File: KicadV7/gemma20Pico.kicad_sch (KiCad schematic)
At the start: 14 parts, among them J1-Prox1 I2C_CH0, J2-Prox0 I2C_CH1, J3-Motor1 DC-Motor, J4-BAT1 3.7V Battery, J5-Servo1 Servo, J6-Pot1 Pot, J7-Pot2 Pot, M1 Motor_DC, M2 Motor_Servo, U1-RPI-Pico1 Pico

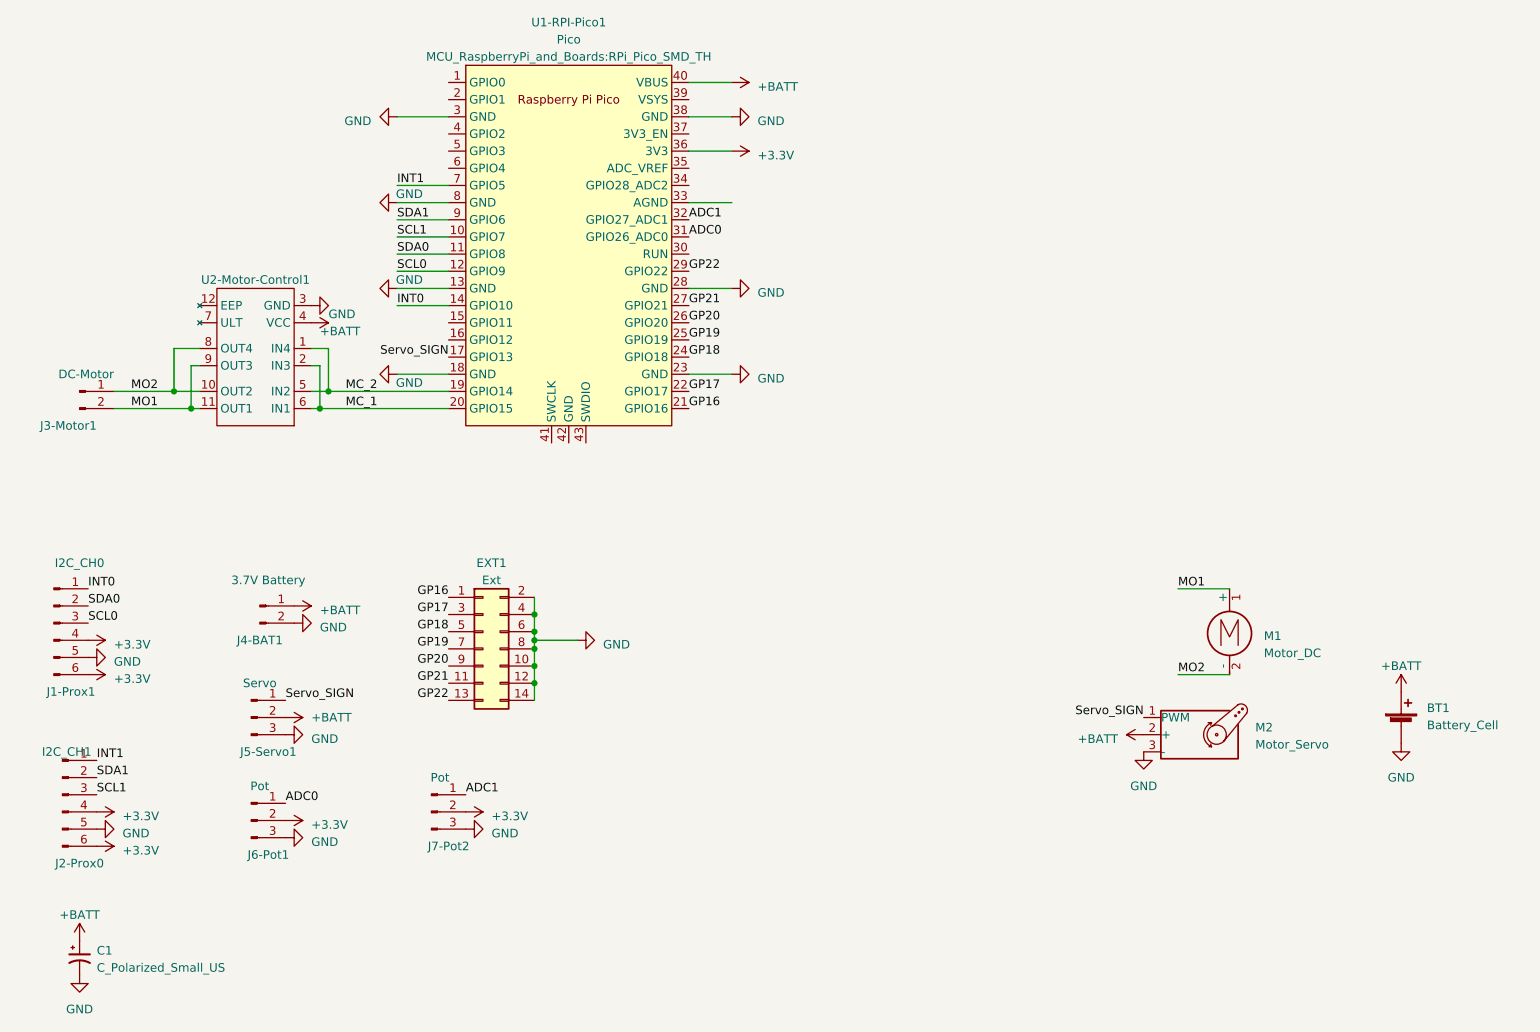
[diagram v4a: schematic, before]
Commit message: Added ECS Pins & cleanup
Added ECS connector allows the DRV8833 to be replaced  with brushless motor controller for RC (also provides +5v)
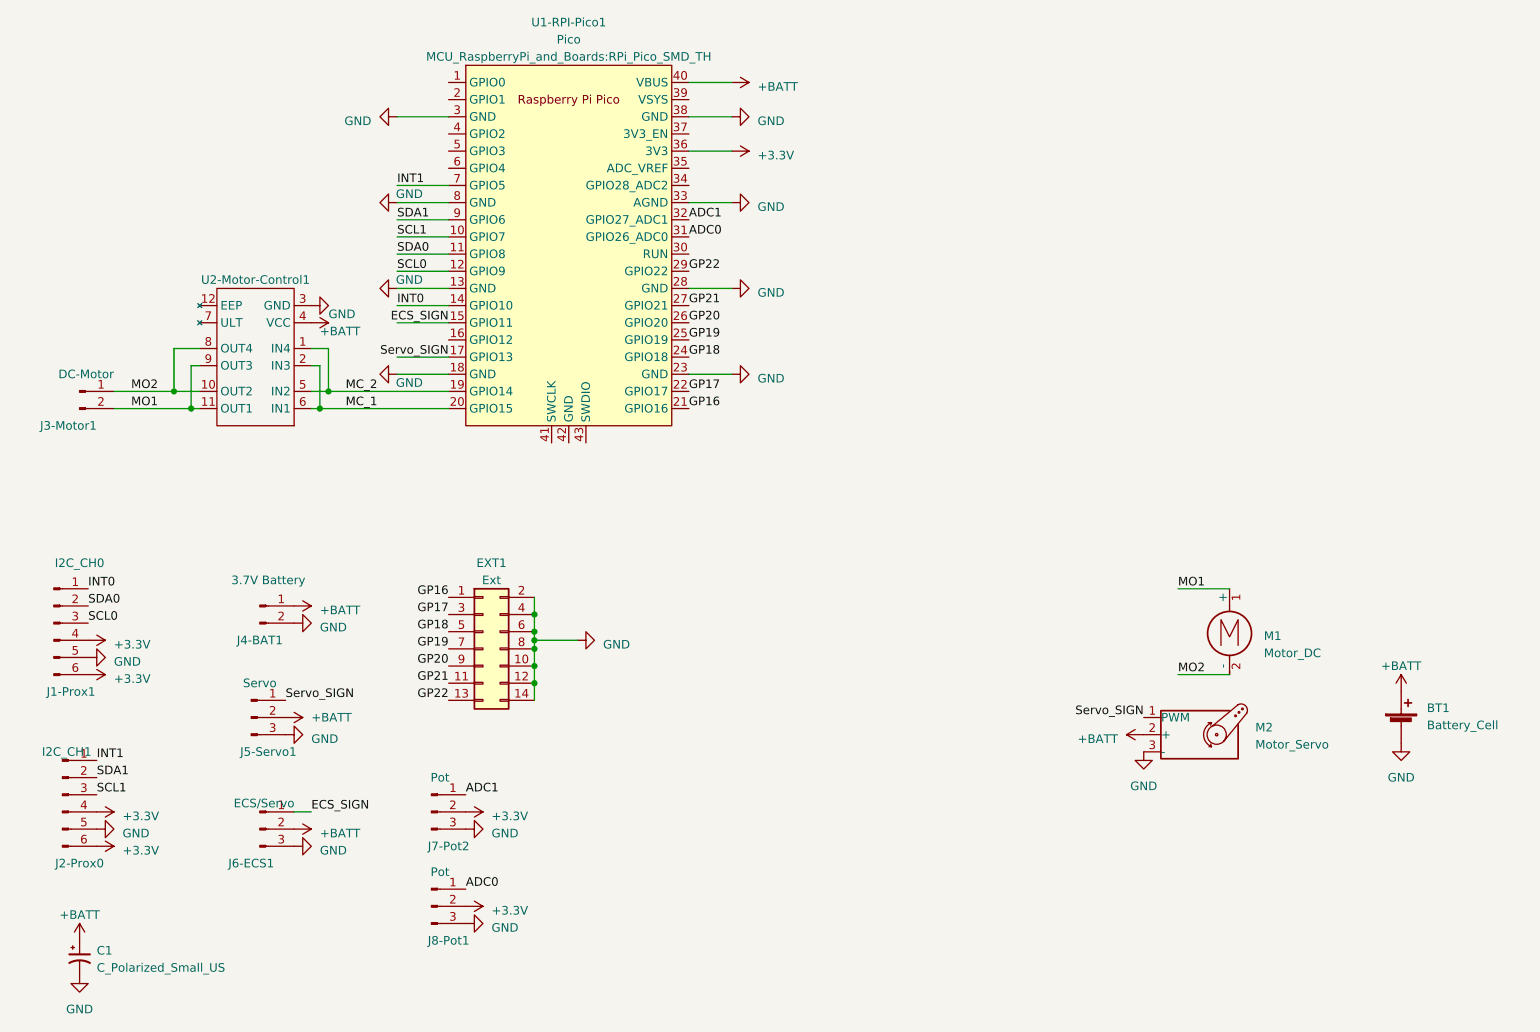
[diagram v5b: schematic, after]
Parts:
- added J6-ECS1: ECS/Servo, Connector_PinHeader_2.54mm:PinHeader_1x03_P2.54mm_Vertical, symbol Connector:Conn_01x03_Pin
- renumbered J6-Pot1 to J8-Pot1
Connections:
- net +BATT: now also J6-ECS1.2 (Pin_2)
- net GND: now also U1-RPI-Pico1.33 (AGND), J6-ECS1.3 (Pin_3)
- net ECS_SIGN: now reaches U1-RPI-Pico1.15 (GPIO11)
- net ECS_SIGN: now also J6-ECS1.1 (Pin_1)
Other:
- moved on the sheet: J8-Pot1
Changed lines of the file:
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@@
+    (stroke (width 0) (type default))
+  )
+  (wire (pts (xy 86.36 83.82) (xy 93.98 83.82))
     (stroke (width 0) (type default))
   )
@@
     (stroke (width 0) (type default))
   )
+  (wire (pts (xy 71.12 151.13) (xy 73.66 151.13))
+    (stroke (width 0) (type default))
+  )
   (wire (pts (xy 76.2 88.9) (xy 93.98 88.9))
     (stroke (width 0) (type default))
@@
   )
   (wire (pts (xy 86.36 71.12) (xy 93.98 71.12))
+    (stroke (width 0) (type default))
+  )
+  (wire (pts (xy 86.36 78.74) (xy 93.98 78.74))
     (stroke (width 0) (type default))
   )
@@
     (effects (font (size 1.27 1.27)) (justify left bottom))
   )
+  (label "ECS_SIGN" (at 93.98 78.74 180) (fields_autoplaced)
+    (effects (font (size 1.27 1.27)) (justify right bottom))
+  )
   (label "GP20" (at 129.54 78.74 0) (fields_autoplaced)
     (effects (font (size 1.27 1.27)) (justify left bottom))
@@
     (effects (font (size 1.27 1.27)) (justify left bottom))
   )
+  (label "ECS_SIGN" (at 73.66 151.13 0) (fields_autoplaced)
+    (effects (font (size 1.27 1.27)) (justify left bottom))
+  )
   (label "INT1" (at 86.36 58.42 0) (fields_autoplaced)
     (effects (font (size 1.27 1.27)) (justify left bottom))
@@
     (effects (font (size 1.27 1.27)) (justify left bottom))
   )
-  (label "ADC0" (at 69.85 149.86 0) (fields_autoplaced)
+  (label "ADC0" (at 96.52 162.56 0) (fields_autoplaced)
     (effects (font (size 1.27 1.27)) (justify left bottom))
   )
@@
     )
   )
-  (symbol (lib_id "power:+3.3V") (at 69.85 152.4 270) (unit 1)
-    (in_bom yes) (on_board yes) (dnp no) (fields_autoplaced)
-    (property "Reference" "#PWR020" (at 66.04 152.4 0)
-      (effects (font (size 1.27 1.27)) hide)
-    )
-    (property "Value" "+3.3V" (at 73.66 153.035 90)
-      (effects (font (size 1.27 1.27)) (justify left))
-    )
-    (property "Footprint" "" (at 69.85 152.4 0)
-      (effects (font (size 1.27 1.27)) hide)
-    )
-    (property "Datasheet" "" (at 69.85 152.4 0)
+  (symbol (lib_id "power:+3.3V") (at 96.52 165.1 270) (unit 1)
+    (in_bom yes) (on_board yes) (dnp no) (fields_autoplaced)
+    (property "Reference" "#PWR020" (at 92.71 165.1 0)
+      (effects (font (size 1.27 1.27)) hide)
+    )
+    (property "Value" "+3.3V" (at 100.33 165.735 90)
+      (effects (font (size 1.27 1.27)) (justify left))
+    )
+    (property "Footprint" "" (at 96.52 165.1 0)
+      (effects (font (size 1.27 1.27)) hide)
+    )
+    (property "Datasheet" "" (at 96.52 165.1 0)
       (effects (font (size 1.27 1.27)) hide)
     )
@@
     )
   )
+  (symbol (lib_id "power:+BATT") (at 71.12 153.67 270) (unit 1)
+    (in_bom yes) (on_board yes) (dnp no) (fields_autoplaced)
+    (property "Reference" "#PWR033" (at 67.31 153.67 0)
+      (effects (font (size 1.27 1.27)) hide)
+    )
+    (property "Value" "+BATT" (at 74.93 154.305 90)
+      (effects (font (size 1.27 1.27)) (justify left))
+    )
+    (property "Footprint" "" (at 71.12 153.67 0)
+      (effects (font (size 1.27 1.27)) hide)
+    )
+    (property "Datasheet" "" (at 71.12 153.67 0)
+      (effects (font (size 1.27 1.27)) hide)
+    )
+    (pin "1")
+    (instances
+      (project "gemma20Pico"
+        (path "/b10b7441-68fa-49c0-9dad-fceb534010fc"
+          (reference "#PWR033") (unit 1)
+        )
+      )
+    )
+  )
   (symbol (lib_id "power:GND") (at 86.36 86.36 270) (unit 1)
     (in_bom yes) (on_board yes) (dnp no)
@@
     )
   )
+  (symbol (lib_id "power:GND") (at 135.89 60.96 90) (unit 1)
+    (in_bom yes) (on_board yes) (dnp no) (fields_autoplaced)
+    (property "Reference" "#PWR035" (at 142.24 60.96 0)
+      (effects (font (size 1.27 1.27)) hide)
+    )
+    (property "Value" "GND" (at 139.7 61.595 90)
+      (effects (font (size 1.27 1.27)) (justify right))
+    )
+    (property "Footprint" "" (at 135.89 60.96 0)
+      (effects (font (size 1.27 1.27)) hide)
+    )
+    (property "Datasheet" "" (at 135.89 60.96 0)
+      (effects (font (size 1.27 1.27)) hide)
+    )
+    (pin "1")
+    (instances
+      (project "gemma20Pico"
+        (path "/b10b7441-68fa-49c0-9dad-fceb534010fc"
+          (reference "#PWR035") (unit 1)
+        )
+      )
+    )
+  )
   (symbol (lib_id "power:GND") (at 86.36 60.96 270) (unit 1)
     (in_bom yes) (on_board yes) (dnp no)
@@
     )
   )
-  (symbol (lib_id "Connector:Conn_01x03_Pin") (at 64.77 152.4 0) (unit 1)
-    (in_bom yes) (on_board yes) (dnp no)
-    (property "Reference" "J6-Pot1" (at 67.31 157.48 0)
-      (effects (font (size 1.27 1.27)))
-    )
-    (property "Value" "Pot" (at 66.04 147.32 0)
-      (effects (font (size 1.27 1.27)))
-    )
-    (property "Footprint" "Connector_PinSocket_2.54mm:PinSocket_1x03_P2.54mm_Vertical" (at 64.77 152.4 0)
-      (effects (font (size 1.27 1.27)) hide)
-    )
-    (property "Datasheet" "~" (at 64.77 152.4 0)
+  (symbol (lib_id "Connector:Conn_01x03_Pin") (at 91.44 165.1 0) (unit 1)
+    (in_bom yes) (on_board yes) (dnp no)
+    (property "Reference" "J8-Pot1" (at 93.98 170.18 0)
+      (effects (font (size 1.27 1.27)))
+    )
+    (property "Value" "Pot" (at 92.71 160.02 0)
+      (effects (font (size 1.27 1.27)))
+    )
+    (property "Footprint" "Connector_PinSocket_2.54mm:PinSocket_1x03_P2.54mm_Vertical" (at 91.44 165.1 0)
+      (effects (font (size 1.27 1.27)) hide)
+    )
+    (property "Datasheet" "~" (at 91.44 165.1 0)
       (effects (font (size 1.27 1.27)) hide)
     )
@@
       (project "gemma20Pico"
         (path "/b10b7441-68fa-49c0-9dad-fceb534010fc"
-          (reference "J6-Pot1") (unit 1)
+          (reference "J8-Pot1") (unit 1)
         )
       )
@@
     )
   )
+  (symbol (lib_id "power:GND") (at 71.12 156.21 90) (unit 1)
+    (in_bom yes) (on_board yes) (dnp no) (fields_autoplaced)
+    (property "Reference" "#PWR034" (at 77.47 156.21 0)
+      (effects (font (size 1.27 1.27)) hide)
+    )
+    (property "Value" "GND" (at 74.93 156.845 90)
+      (effects (font (size 1.27 1.27)) (justify right))
+    )
+    (property "Footprint" "" (at 71.12 156.21 0)
+      (effects (font (size 1.27 1.27)) hide)
+    )
+    (property "Datasheet" "" (at 71.12 156.21 0)
+      (effects (font (size 1.27 1.27)) hide)
+    )
+    (pin "1")
+    (instances
+      (project "gemma20Pico"
+        (path "/b10b7441-68fa-49c0-9dad-fceb534010fc"
+          (reference "#PWR034") (unit 1)
+        )
+      )
+    )
+  )
   (symbol (lib_id "Connector:Conn_01x02_Pin") (at 66.04 120.65 0) (unit 1)
     (in_bom yes) (on_board yes) (dnp no)
@@
     )
   )
-  (symbol (lib_id "power:GND") (at 69.85 154.94 90) (unit 1)
-    (in_bom yes) (on_board yes) (dnp no) (fields_autoplaced)
-    (property "Reference" "#PWR021" (at 76.2 154.94 0)
-      (effects (font (size 1.27 1.27)) hide)
-    )
-    (property "Value" "GND" (at 73.66 155.575 90)
-      (effects (font (size 1.27 1.27)) (justify right))
-    )
-    (property "Footprint" "" (at 69.85 154.94 0)
-      (effects (font (size 1.27 1.27)) hide)
-    )
-    (property "Datasheet" "" (at 69.85 154.94 0)
+  (symbol (lib_id "power:GND") (at 96.52 167.64 90) (unit 1)
+    (in_bom yes) (on_board yes) (dnp no) (fields_autoplaced)
+    (property "Reference" "#PWR021" (at 102.87 167.64 0)
+      (effects (font (size 1.27 1.27)) hide)
+    )
+    (property "Value" "GND" (at 100.33 168.275 90)
+      (effects (font (size 1.27 1.27)) (justify right))
+    )
+    (property "Footprint" "" (at 96.52 167.64 0)
+      (effects (font (size 1.27 1.27)) hide)
+    )
+    (property "Datasheet" "" (at 96.52 167.64 0)
       (effects (font (size 1.27 1.27)) hide)
     )
@@
         )
       )
+    )
+  )
+  (symbol (lib_id "Connector:Conn_01x03_Pin") (at 66.04 153.67 0) (unit 1)
+    (in_bom yes) (on_board yes) (dnp no)
+    (property "Reference" "J6-ECS1" (at 64.77 158.75 0)
+      (effects (font (size 1.27 1.27)))
+    )
+    (property "Value" "ECS/Servo" (at 66.675 149.86 0)
+      (effects (font (size 1.27 1.27)))
+    )
+    (property "Footprint" "Connector_PinHeader_2.54mm:PinHeader_1x03_P2.54mm_Vertical" (at 66.04 153.67 0)
+      (effects (font (size 1.27 1.27)) hide)
+    )
+    (property "Datasheet" "~" (at 66.04 153.67 0)
+      (effects (font (size 1.27 1.27)) hide)
+    )
+    (pin "1")
+    (pin "2")
+    (pin "3")
+    (instances
+      (project "gemma20Pico"
+        (path "/b10b7441-68fa-49c0-9dad-fceb534010fc"
+          (reference "J6-ECS1") (unit 1)
+        )
+      )
